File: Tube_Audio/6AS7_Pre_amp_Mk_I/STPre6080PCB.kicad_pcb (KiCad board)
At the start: 2 copper layers, 168.9 x 71.1 mm, 54 parts, among them J101 Screw_Terminal_01x02, J102 Screw_Terminal_01x04, J103 Screw_Terminal_01x03, J203 Screw_Terminal_01x03, Q101 ZVN0545A, Q102 ZVN0545A, Q201 ZVN0545A, Q202 ZVN0545A

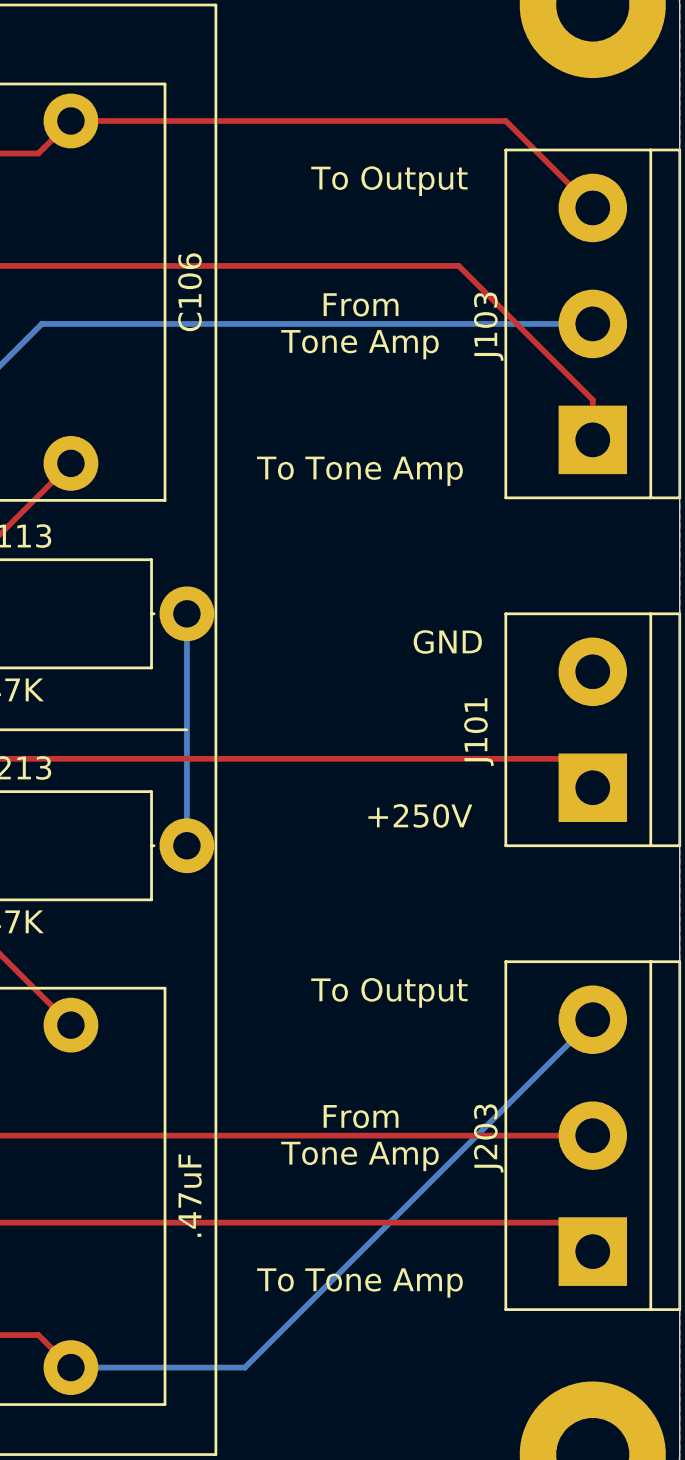
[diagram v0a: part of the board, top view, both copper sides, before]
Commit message: Add high voltage warnings.
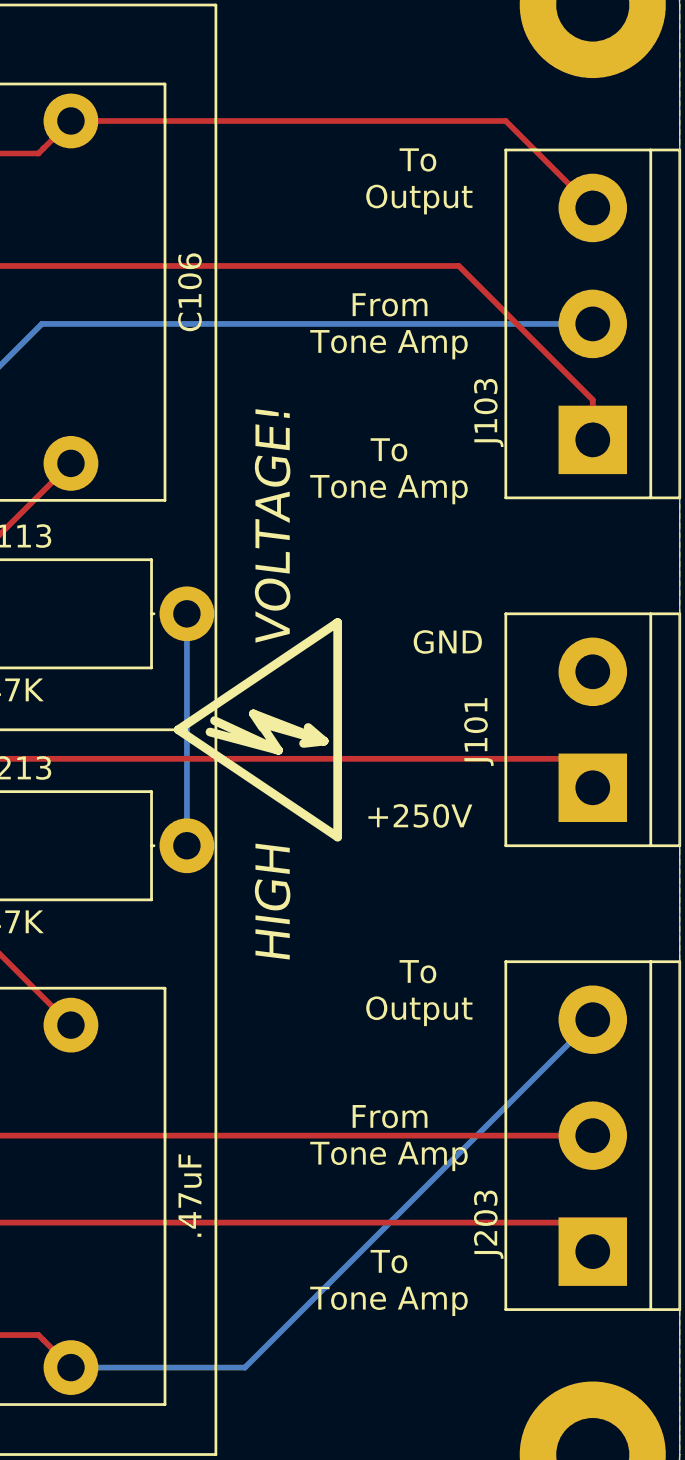
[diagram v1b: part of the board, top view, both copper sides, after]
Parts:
- added REF**: Symbol_HighVoltage_Type2_CopperTop_VerySmall, jrt-Graphics:Symbol_HighVoltage_Type2_FSilk_VerySmall, F.Cu at (191.8, 115.6)
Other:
- board text added: "HIGH"
- board text added: "VOLTAGE!"
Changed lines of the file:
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@@
   (general
     (thickness 1.6)
-    (drawings 50)
+    (drawings 52)
     (tracks 154)
     (zones 0)
-    (modules 54)
+    (modules 55)
     (nets 39)
   )
@@
     (add_net R_tone_output)
   )
+  (module jrt-Graphics:Symbol_HighVoltage_Type2_FSilk_VerySmall (layer F.Cu)
+    (at 191.77 115.57 90)
+    (descr "Symbol, High Voltage, Type 2, Copper Top, Very Small,")
+    (tags "Symbol, High Voltage, Type 2, Copper Top, Very Small,")
+    (attr virtual)
+    (fp_text reference REF** (at -0.127 -5.715 90) (layer F.SilkS) hide
+      (effects (font (size 1 1) (thickness 0.15)))
+    )
+    (fp_text value Symbol_HighVoltage_Type2_CopperTop_VerySmall (at -0.381 4.572 90) (layer F.Fab) hide
+      (effects (font (size 1 1) (thickness 0.15)))
+    )
+    (fp_line (start -4.699 2.794) (end 0 -4.191) (layer F.SilkS) (width 0.381))
+    (fp_line (start 4.699 2.794) (end -4.699 2.794) (layer F.SilkS) (width 0.381))
+    (fp_line (start 0 -4.191) (end 4.699 2.794) (layer F.SilkS) (width 0.381))
+    (fp_line (start -0.49784 2.19964) (end -0.59944 1.30048) (layer F.SilkS) (width 0.381))
+    (fp_line (start 0.29972 -0.59944) (end -0.49784 2.19964) (layer F.SilkS) (width 0.381))
+    (fp_line (start -0.89916 0.20066) (end 0.29972 -0.59944) (layer F.SilkS) (width 0.381))
+    (fp_line (start -0.09906 -2.79908) (end -0.89916 0.20066) (layer F.SilkS) (width 0.381))
+    (fp_line (start -0.49784 2.19964) (end 0.1016 1.50114) (layer F.SilkS) (width 0.381))
+    (fp_line (start -0.89916 0.20066) (end 0.40132 -2.60096) (layer F.SilkS) (width 0.381))
+    (fp_line (start 0.70104 -0.89916) (end 0.1016 -0.50038) (layer F.SilkS) (width 0.381))
+    (fp_line (start -0.49784 2.19964) (end 0.70104 -0.89916) (layer F.SilkS) (width 0.381))
+  )
   (module Package_TO_SOT_THT:TO-92_Wide (layer F.Cu)
     (at 88.9 97.79 270)
@@
     (descr "simple 3-pin terminal block, pitch 5.08mm, revamped version of bornier3")
     (tags "terminal block bornier3")
-    (fp_text reference J103 (at 5.05 -4.65 90) (layer F.SilkS)
+    (fp_text reference J103 (at 1.27 -4.65 90) (layer F.SilkS)
       (effects (font (size 1 1) (thickness 0.15)))
     )
@@
     (descr "simple 3-pin terminal block, pitch 5.08mm, revamped version of bornier3")
     (tags "terminal block bornier3")
-    (fp_text reference J203 (at 5.05 -4.65 90) (layer F.SilkS)
+    (fp_text reference J203 (at 1.27 -4.65 90) (layer F.SilkS)
       (effects (font (size 1 1) (thickness 0.15)))
     )
@@
     )
   )
+  (gr_text VOLTAGE! (at 191.77 106.68 90) (layer F.SilkS)
+    (effects (font (size 1.5 1.5) (thickness 0.3) italic))
+  )
+  (gr_text HIGH (at 191.77 123.19 90) (layer F.SilkS)
+    (effects (font (size 1.5 1.5) (thickness 0.3) italic))
+  )
   (dimension 63.5 (width 0.15) (layer Dwgs.User)
     (gr_text "63.500 mm" (at 34.26 115.57 270) (layer Dwgs.User)
@@
   (gr_line (start 157.48 147.32) (end 189.23 147.32) (layer F.SilkS) (width 0.12))
   (gr_line (start 157.48 83.82) (end 189.23 83.82) (layer F.SilkS) (width 0.12))
-  (gr_text "To Tone Amp" (at 195.58 139.7) (layer F.SilkS)
+  (gr_text "To\nTone Amp" (at 196.85 139.7) (layer F.SilkS)
     (effects (font (size 1 1) (thickness 0.15)))
   )
-  (gr_text "From\nTone Amp" (at 195.58 133.35) (layer F.SilkS)
+  (gr_text "From\nTone Amp" (at 196.85 133.35) (layer F.SilkS)
     (effects (font (size 1 1) (thickness 0.15)))
   )
-  (gr_text "To Output" (at 196.85 127) (layer F.SilkS)
+  (gr_text "To\nOutput" (at 198.12 127) (layer F.SilkS)
     (effects (font (size 1 1) (thickness 0.15)))
   )
-  (gr_text "To Output" (at 196.85 91.44) (layer F.SilkS)
+  (gr_text "To\nOutput" (at 198.12 91.44) (layer F.SilkS)
     (effects (font (size 1 1) (thickness 0.15)))
   )
-  (gr_text "From\nTone Amp" (at 195.58 97.79) (layer F.SilkS)
+  (gr_text "From\nTone Amp" (at 196.85 97.79) (layer F.SilkS)
     (effects (font (size 1 1) (thickness 0.15)))
   )
-  (gr_text "To Tone Amp" (at 195.58 104.14) (layer F.SilkS)
+  (gr_text "To\nTone Amp" (at 196.85 104.14) (layer F.SilkS)
     (effects (font (size 1 1) (thickness 0.15)))
   )
